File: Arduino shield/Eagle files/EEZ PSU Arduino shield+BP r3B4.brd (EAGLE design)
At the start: 207 x 74 mm, 185 parts, among them IC20 TLC5925IDBQR, IC21 Si8641EC-B-IS1, IC22 SI8651EC-B-IS1, IC23 SI8651EC-B-IS1, IC24 LD1117ADT33TR, IC25 Si8641EC-B-IS1, IC26 PCA21125T/Q900/1,1, IC27 AT25256B-SSHL-B, IC28 W5500, IC29 BC857BS, IC30 TLC555, IC31 SN74LVC2G08DCTR, IC32 TPS3705-33D, IC33 SN74LV1T34DBVR, IC34 SN74LVC2G02DCTR, J1 BS-244DSM-R, J2 BS-244DSM-G, J3 BS-244DSM-B, J4 BS-244DSM-R, J5 BS-244DSM-B, Q23 IRLML2246TRPBF, Q24 IRLML2246TRPBF, Q25 IRLML2246TRPBF, Q26 IRLML2246TRPBF, Q27 2N7002, Q28 IRLML2246TRPBF, Q29 2N7002, Q30 2N7002, SW1 A101SYCQ04, SW2 1301.9316, X12 MC000006, X13 TSW-113-07-F-D, X14 MC000005, X15 TSW-113-07-F-D, X16 09185067324, X17 22-23-2021, X18 826629-8, X19 22-23-2041, X20 SSW-105-02-S-D, Y1 32,768kHz, Y2 25MHz

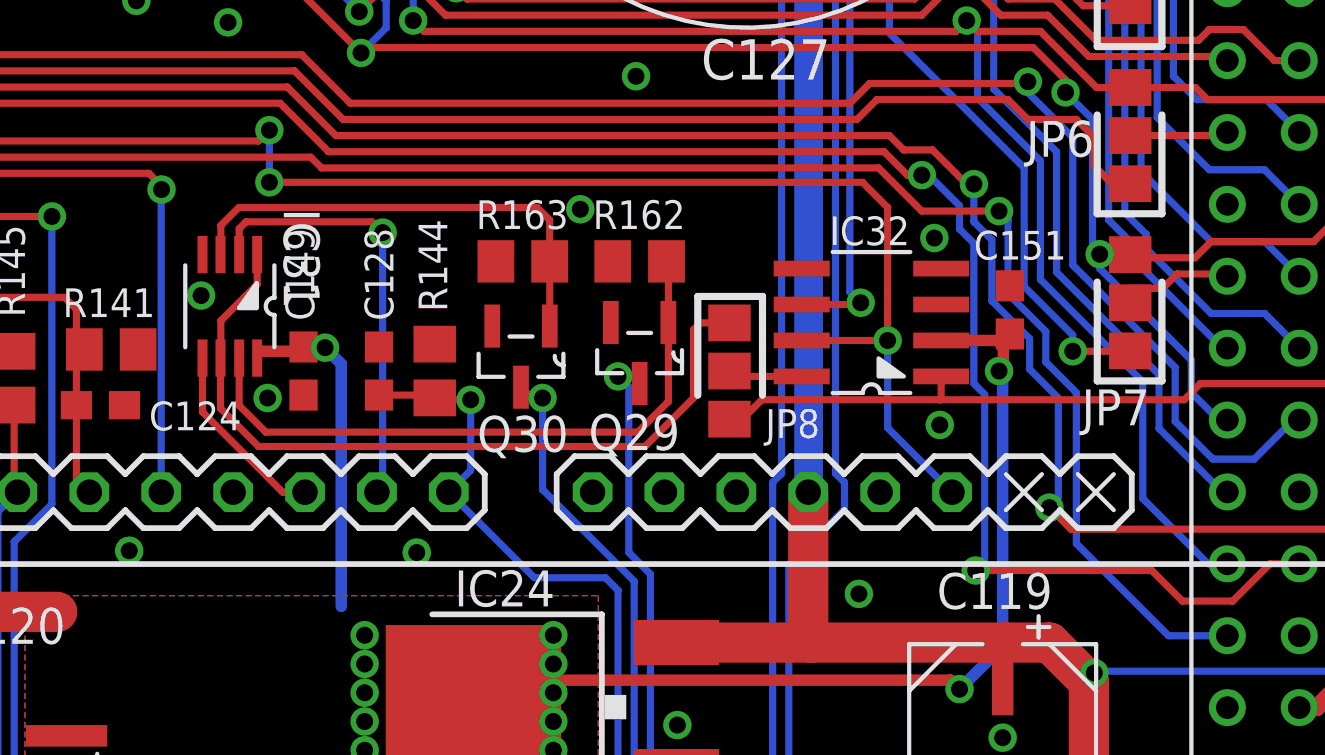
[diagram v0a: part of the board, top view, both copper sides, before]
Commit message: Small corrections on top silkscreen
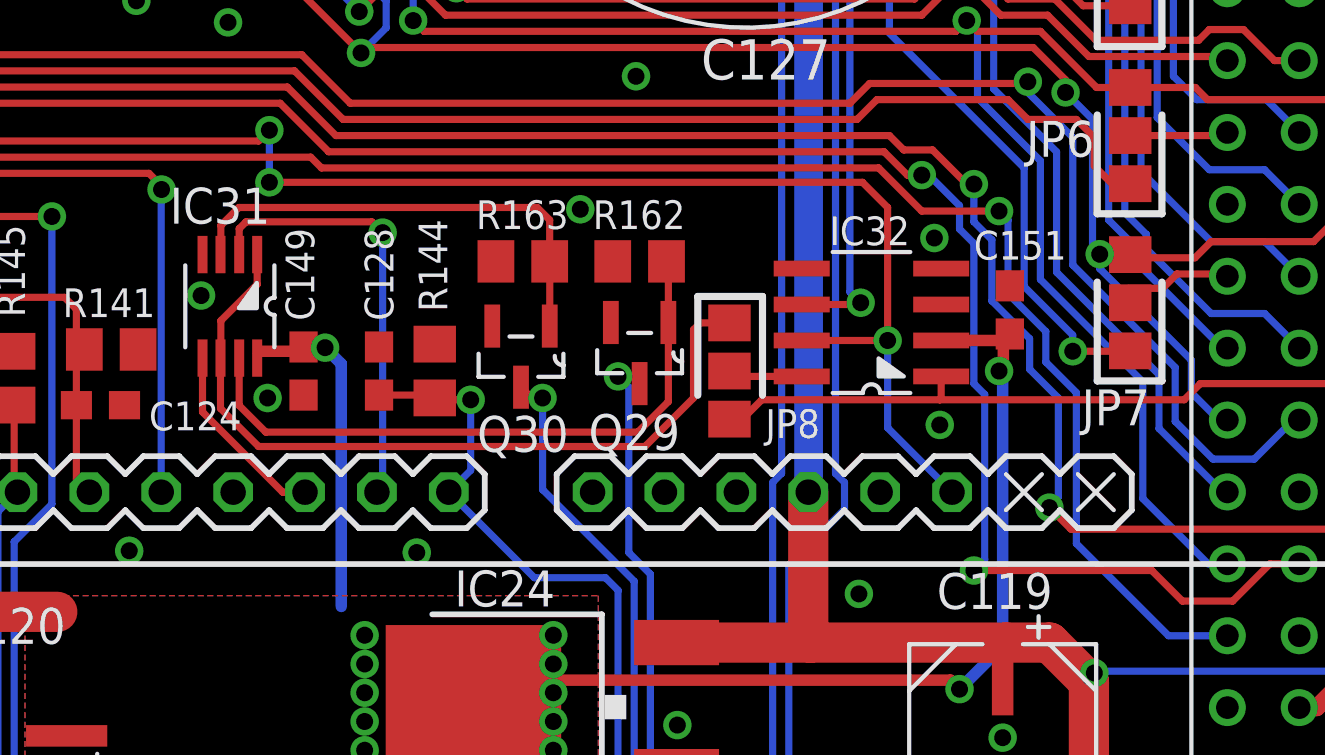
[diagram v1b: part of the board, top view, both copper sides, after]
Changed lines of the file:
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@@
 <layer number="27" name="tValues" color="10" fill="1" visible="no" active="yes"/>
 <layer number="28" name="bValues" color="11" fill="1" visible="no" active="yes"/>
-<layer number="29" name="tStop" color="7" fill="3" visible="yes" active="yes"/>
+<layer number="29" name="tStop" color="7" fill="3" visible="no" active="yes"/>
 <layer number="30" name="bStop" color="7" fill="6" visible="no" active="yes"/>
 <layer number="31" name="tCream" color="7" fill="4" visible="no" active="yes"/>
@@
 <layer number="37" name="tTest" color="7" fill="1" visible="no" active="yes"/>
 <layer number="38" name="bTest" color="7" fill="1" visible="no" active="yes"/>
-<layer number="39" name="tKeepout" color="15" fill="1" visible="yes" active="yes"/>
+<layer number="39" name="tKeepout" color="15" fill="1" visible="no" active="yes"/>
 <layer number="40" name="bKeepout" color="13" fill="1" visible="no" active="yes"/>
 <layer number="41" name="tRestrict" color="4" fill="10" visible="no" active="yes"/>
@@
 <layer number="123" name="tTestmark" color="7" fill="1" visible="no" active="no"/>
 <layer number="124" name="bTestmark" color="7" fill="1" visible="no" active="no"/>
-<layer number="125" name="_tNames" color="14" fill="1" visible="no" active="yes"/>
+<layer number="125" name="_tNames" color="14" fill="1" visible="yes" active="yes"/>
 <layer number="126" name="_bNames" color="5" fill="1" visible="no" active="yes"/>
 <layer number="127" name="_tValues" color="7" fill="1" visible="no" active="no"/>
@@
 <text x="187.4266" y="47.4345" size="1.016" layer="125" ratio="10" rot="SR0">IC29</text>
 <text x="198.9836" y="46.1645" size="1.016" layer="125" ratio="10" rot="SR0">IC30</text>
-<text x="269.621" y="33.1724" size="1.27" layer="125" ratio="10" rot="SR270">IC31</text>
+<text x="265.5951" y="32.639" size="1.27" layer="125" ratio="10" rot="SR0">IC31</text>
 <text x="288.8996" y="31.877" size="1.016" layer="125" ratio="10" rot="SR0">IC32</text>
 <text x="198.4756" y="61.7855" size="1.27" layer="125" ratio="10">IC33</text>
@@
 <attribute name="SUPPLIER" value="Texas Instruments" x="267.716" y="29.718" size="1.778" layer="27" rot="R270" display="off"/>
 <attribute name="OC_FARNELL" value="1470871" x="267.716" y="29.718" size="1.778" layer="27" rot="R270" display="off"/>
-<attribute name="NAME" x="269.621" y="33.1724" size="1.27" layer="25" ratio="10" rot="SR270"/>
+<attribute name="NAME" x="265.5951" y="32.639" size="1.27" layer="25" ratio="10" rot="SR0"/>
 <attribute name="VALUE" x="267.208" y="34.2519" size="0.8128" layer="27" ratio="10" rot="SR270"/>
 </element>
@@
 <contactref element="MCU" pad="38"/>
 <contactref element="LCD1" pad="17"/>
-<via x="294.0685" y="20.3835" extent="1-16" drill="0.6" shape="octagon"/>
-<wire x1="294.0685" y1="20.3835" x2="300.2915" y2="20.3835" width="0.254" layer="1"/>
+<via x="294.005" y="20.3835" extent="1-16" drill="0.6" shape="octagon"/>
+<wire x1="294.005" y1="20.3835" x2="300.2915" y2="20.3835" width="0.254" layer="1"/>
 <wire x1="300.2915" y1="20.3835" x2="301.371" y2="19.304" width="0.254" layer="1"/>
 <wire x1="301.371" y1="19.304" x2="303.149" y2="19.304" width="0.254" layer="1"/>
@@
 <wire x1="292.1635" y1="34.3535" x2="291.6555" y2="34.3535" width="0.254" layer="1"/>
 <wire x1="291.6555" y1="34.3535" x2="290.83" y2="35.179" width="0.254" layer="1"/>
-<wire x1="294.0685" y1="20.3835" x2="294.386" y2="20.701" width="0.254" layer="16"/>
-<wire x1="294.386" y1="20.701" x2="294.386" y2="26.6065" width="0.254" layer="16"/>
+<wire x1="294.005" y1="20.3835" x2="294.386" y2="20.7645" width="0.254" layer="16"/>
+<wire x1="294.386" y1="20.7645" x2="294.386" y2="26.6065" width="0.254" layer="16"/>
 <wire x1="294.386" y1="26.6065" x2="294.005" y2="26.9875" width="0.254" layer="16"/>
 <wire x1="294.005" y1="26.9875" x2="294.005" y2="31.9405" width="0.254" layer="16"/>
@@
 </signal>
 </signals>
+<errors>
+</errors>
 </board>
 </drawing>

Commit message: X18 type changed
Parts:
- X18: value 826629-8 -> MC34753
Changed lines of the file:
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@@
 <attribute name="VALUE" x="207.4545" y="61.087" size="1.016" layer="27" ratio="10" rot="R180"/>
 </element>
-<element name="X18" library="con-samtec" package="SSW-108-02-S-S" value="826629-8" x="209.931" y="14.5415" smashed="yes" rot="R90">
+<element name="X18" library="con-samtec" package="SSW-108-02-S-S" value="MC34753" x="209.931" y="14.5415" smashed="yes" rot="R90">
 <attribute name="OC_NEWARK" value="11P9448" x="209.931" y="14.5415" size="1.778" layer="27" rot="R90" display="off"/>
 <attribute name="MPN" value="SSW-108-02-S-S" x="209.931" y="14.5415" size="1.778" layer="27" rot="R90" display="off"/>
@@
 </signal>
 </signals>
-<errors>
-</errors>
 </board>
 </drawing>
